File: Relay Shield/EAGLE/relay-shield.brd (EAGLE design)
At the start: 88.9 x 83.8 mm, 46 parts, among them J1 POWER_JACKSLT, Q1 MPSA42, Q2 MPSA42, Q3 MPSA42, Q4 MPSA42, U1 RELAYPANASONIC-JS, U2 RELAYPANASONIC-JS, U3 RELAYPANASONIC-JS, U4 RELAYPANASONIC-JS, U5 SPARK_CORE, U6 AP1509-50SG-13

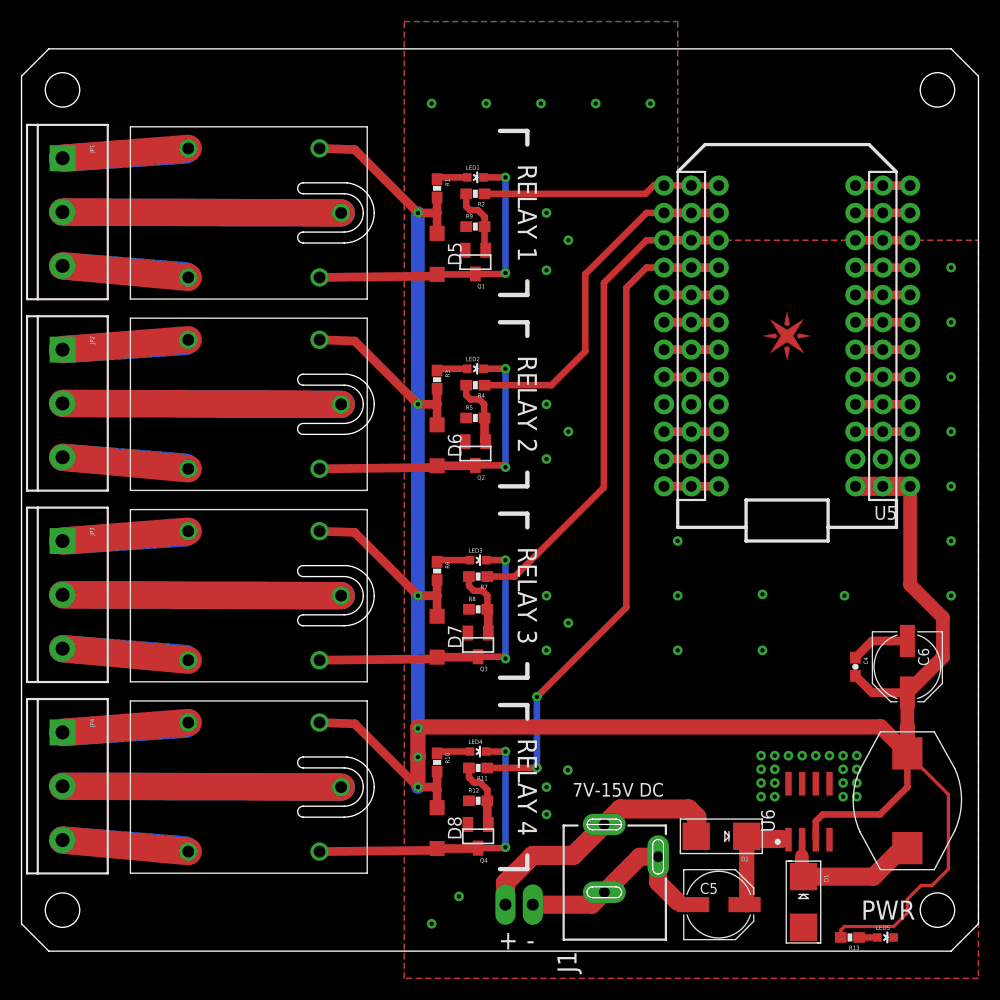
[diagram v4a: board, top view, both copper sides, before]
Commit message: updated relay shield files to v210
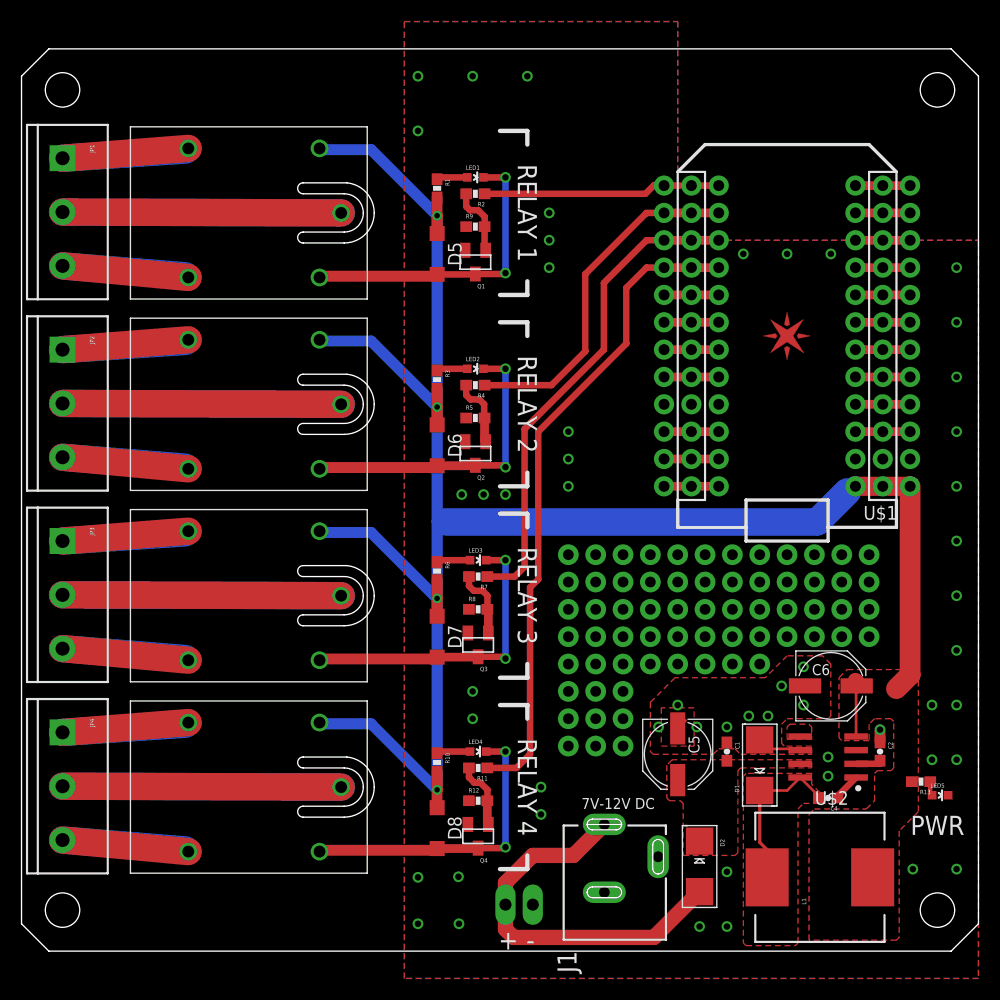
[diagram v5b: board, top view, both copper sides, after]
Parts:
- removed U6: AP1509-50SG-13, Spark:SO08
- added C1: 0.1uF, SparkFun-Capacitors:0603-CAP
- added C2: 10nF, SparkFun-Capacitors:0603-CAP
- added U$2: LM2672, Spark:SO08
- C5: value 47uF, 25V -> 100uF, 16V
- C6: value 100uF, 10V -> 56uF, 10V
- L1: value SDR1005-470KL -> CDRH125NP-470M; device Spark:INDUCTOR-SDR1005-470KL -> SparkFun-Passives:CDRH125
- moved R13 15.9 mm to (83.6, 15.7)
- moved C5 14.5 mm to (61.0, 18.3), turned to 270 degrees
- moved LED5 14.2 mm to (85.3, 14.5)
- moved D1 13.3 mm to (68.6, 17.3), turned to 90 degrees
- moved C4 12.5 mm to (74.9, 14.2), turned to 180 degrees
- moved L1 10.8 mm to (74.2, 6.86)
- moved C6 7.33 mm to (75.2, 24.6), turned to 0 degrees
- moved D2 3.45 mm to (63.0, 7.87), turned to 270 degrees
- renumbered U5 to U$1
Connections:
- new net N$33: C4.1, U$2.1
- new net N$35: U$2.5
- new net N$36: C2.2, U$2.2
- net +5V: now also L1.2, U$2.4; no longer C4.2, L1.P$2, U6.3
- net GND: now also C1.1, C2.1, U$2.6; no longer C4.1, U6.4, U6.5, U6.6, U6.7, U6.8
- net N$14: now also C1.2, U$2.7; no longer U6.1
- net N$34: now also C4.2, L1.1, U$2.8; no longer L1.P$1, U6.2
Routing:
- net +5V: track 257.8 -> 191.0 mm, vias 6 -> 4
- net GND: track 25.4 -> 7.21 mm, vias 52 -> 53
- net N$32: track 24.8 -> 35.9 mm
- net N$14: track 10.6 -> 0.52 mm
- net N$36: track 0.00 -> 2.91 mm
- net N$33: track 0.00 -> 2.78 mm
- net N$34: track 16.5 -> 15.2 mm
- net RELAY4: track 62.0 -> 60.9 mm, vias 2 -> 0
- added copper zone on layer 1, net +5V
- added copper zone on layer 1, net N$14
- added copper zone on layer 1, net N$34
- added copper zone on layer 1, net N$35
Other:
- board text added: "7V-12V DC"
- board text added: "Relay Shield v2.1.0 spark.io"
- board text removed: "7V-15V DC"
- board text removed: "Reference Designs ARE PROVIDED "AS IS" AND "WITH ALL FAULTS. SPARK LABS, INC ("SPARK") DISCLAIMS ALL OTHER WARRANTIES, EXPRESS OR IMPLIED, REGARDING PRODUCTS OR THE REFERENCE DESIGNS, INCLUDING BUT NOT LIMITED TO, ANY IMPLIED WARRANTIES OF MERCHANTABILITY, FITNESS FOR A PARTICULAR PURPOSE, OR NON-INFRINGEMENT. Spark may make changes to specifications and product descriptions at any time, without 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"
- board text removed: "Relay Shield v2.0.1 spark.io"

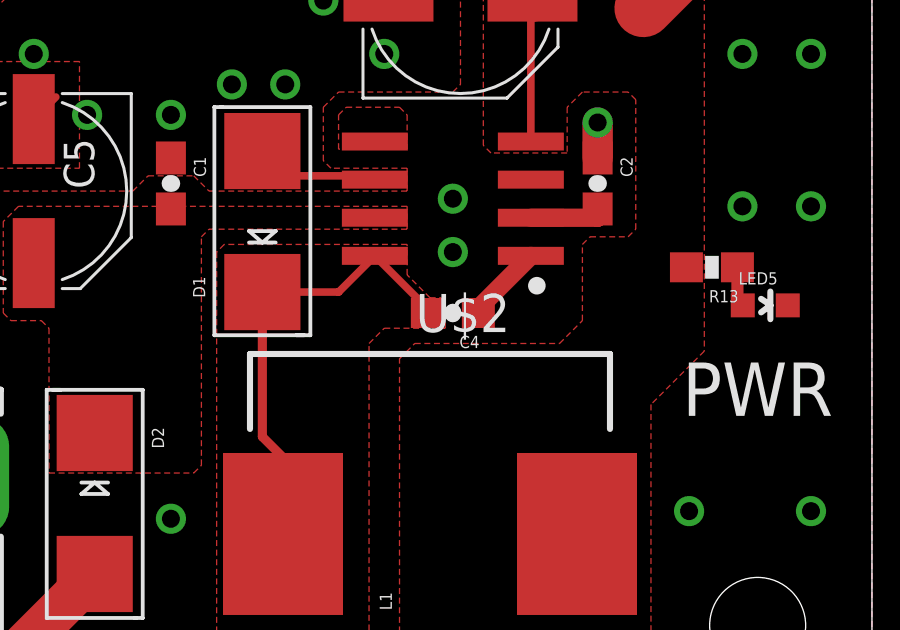
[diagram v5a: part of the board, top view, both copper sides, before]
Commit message: updated the bom and designator for regulator
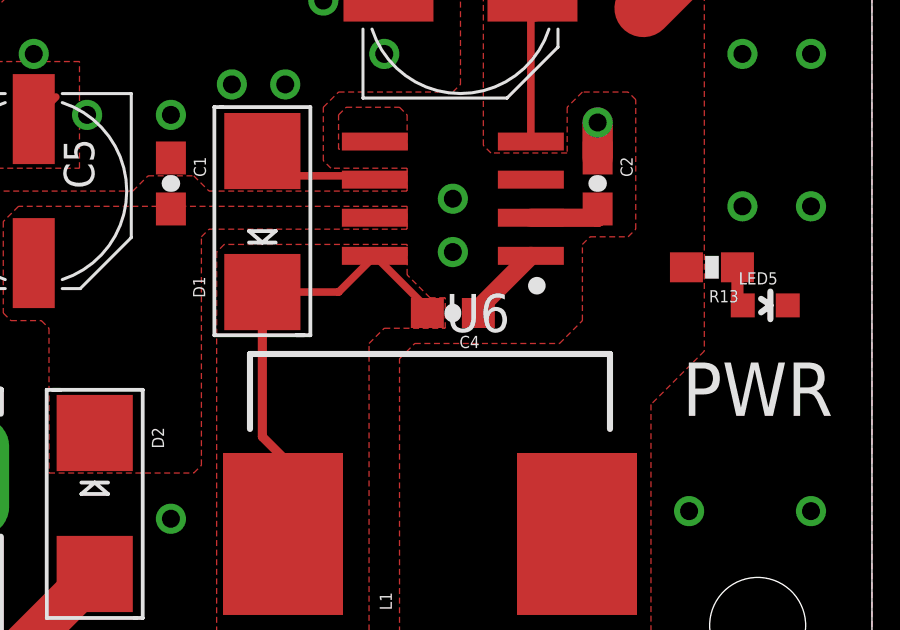
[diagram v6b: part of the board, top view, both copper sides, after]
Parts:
- renumbered U$2 to U6
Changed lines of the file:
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@@
 <element name="D1" library="adafruit" package="SMADIODE" value="B230" x="68.58" y="17.272" rot="R90"/>
 <element name="D2" library="adafruit" package="SMADIODE" value="B230" x="62.992" y="7.874" rot="R270"/>
-<element name="U$2" library="Spark" package="SO08" value="LM2672" x="74.93" y="18.034" rot="R90"/>
+<element name="U6" library="Spark" package="SO08" value="LM2672" x="74.93" y="18.034" rot="R90"/>
 <element name="C1" library="SparkFun-Capacitors" package="0603-CAP" value="0.1uF" x="65.532" y="18.542" rot="R270">
 <attribute name="PROD_ID" value="CAP-08604" x="65.532" y="18.542" size="1.778" layer="27" rot="R270" display="off"/>
@@
 <contactref element="Q3" pad="2"/>
 <contactref element="Q4" pad="2"/>
-<contactref element="U$2" pad="6"/>
-<contactref element="U$2" pad="6"/>
+<contactref element="U6" pad="6"/>
+<contactref element="U6" pad="6"/>
 <contactref element="C5" pad="-"/>
 <contactref element="J1" pad="GND@1"/>
@@
 <contactref element="D7" pad="C"/>
 <contactref element="D8" pad="C"/>
-<contactref element="U$2" pad="4"/>
+<contactref element="U6" pad="4"/>
 <contactref element="C6" pad="+"/>
 <contactref element="R13" pad="2"/>
@@
 <signal name="N$14">
 <contactref element="C5" pad="+"/>
-<contactref element="U$2" pad="7"/>
+<contactref element="U6" pad="7"/>
 <contactref element="D2" pad="C"/>
 <contactref element="C1" pad="2"/>
@@
 </signal>
 <signal name="N$33">
-<contactref element="U$2" pad="1"/>
+<contactref element="U6" pad="1"/>
 <contactref element="C4" pad="1"/>
 <wire x1="77.53" y1="15.974" x2="77.53" y2="16.129" width="0.254" layer="1"/>
@@
 </signal>
 <signal name="N$34">
-<contactref element="U$2" pad="8"/>
+<contactref element="U6" pad="8"/>
 <contactref element="D1" pad="C"/>
 <contactref element="C4" pad="2"/>
@@
 </signal>
 <signal name="N$35">
-<contactref element="U$2" pad="5"/>
+<contactref element="U6" pad="5"/>
 <polygon width="0" layer="1" spacing="6.4516" thermals="no">
 <vertex x="71.12" y="19.685"/>
@@
 <signal name="N$36">
 <contactref element="C2" pad="2"/>
-<contactref element="U$2" pad="2"/>
+<contactref element="U6" pad="2"/>
 <wire x1="80.01" y1="17.399" x2="79.756" y2="17.692" width="0.4064" layer="1"/>
 <wire x1="77.53" y1="17.399" x2="79.756" y2="17.399" width="0.6096" layer="1"/>

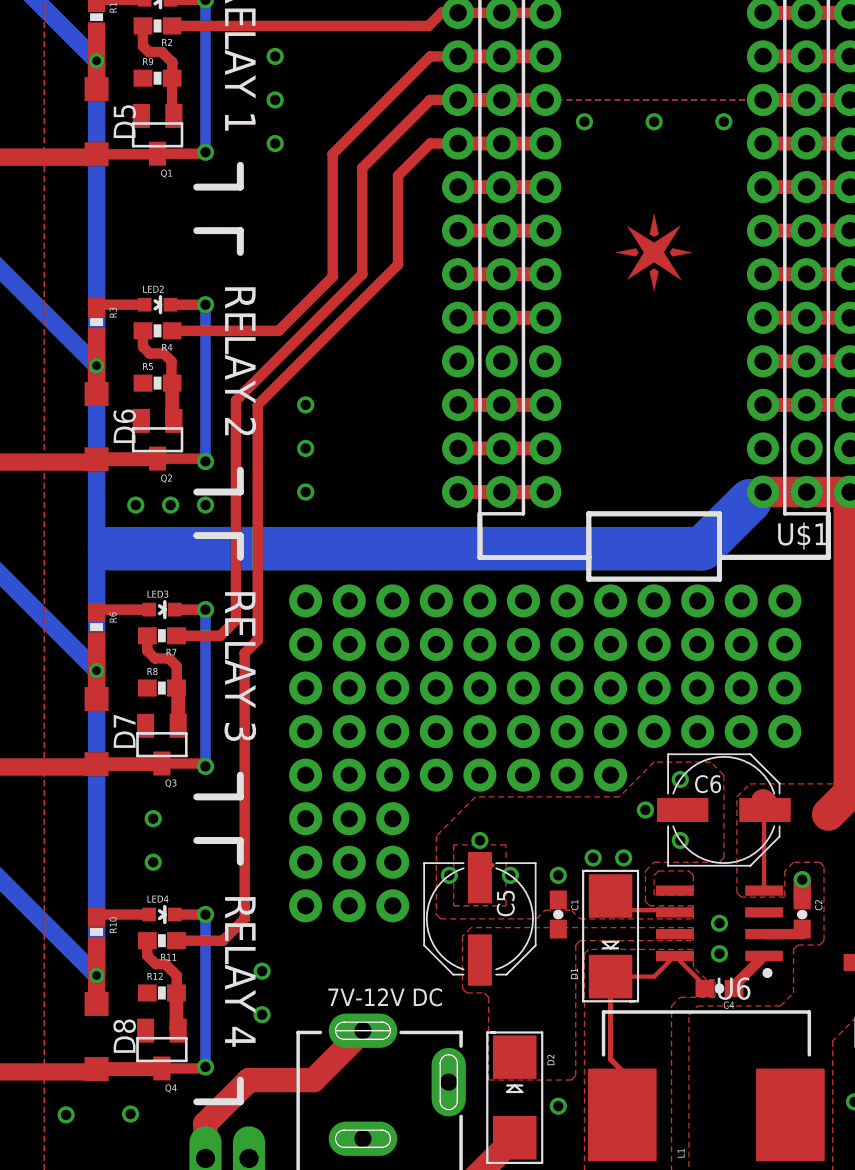
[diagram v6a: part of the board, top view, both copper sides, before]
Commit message: updated designators and bom
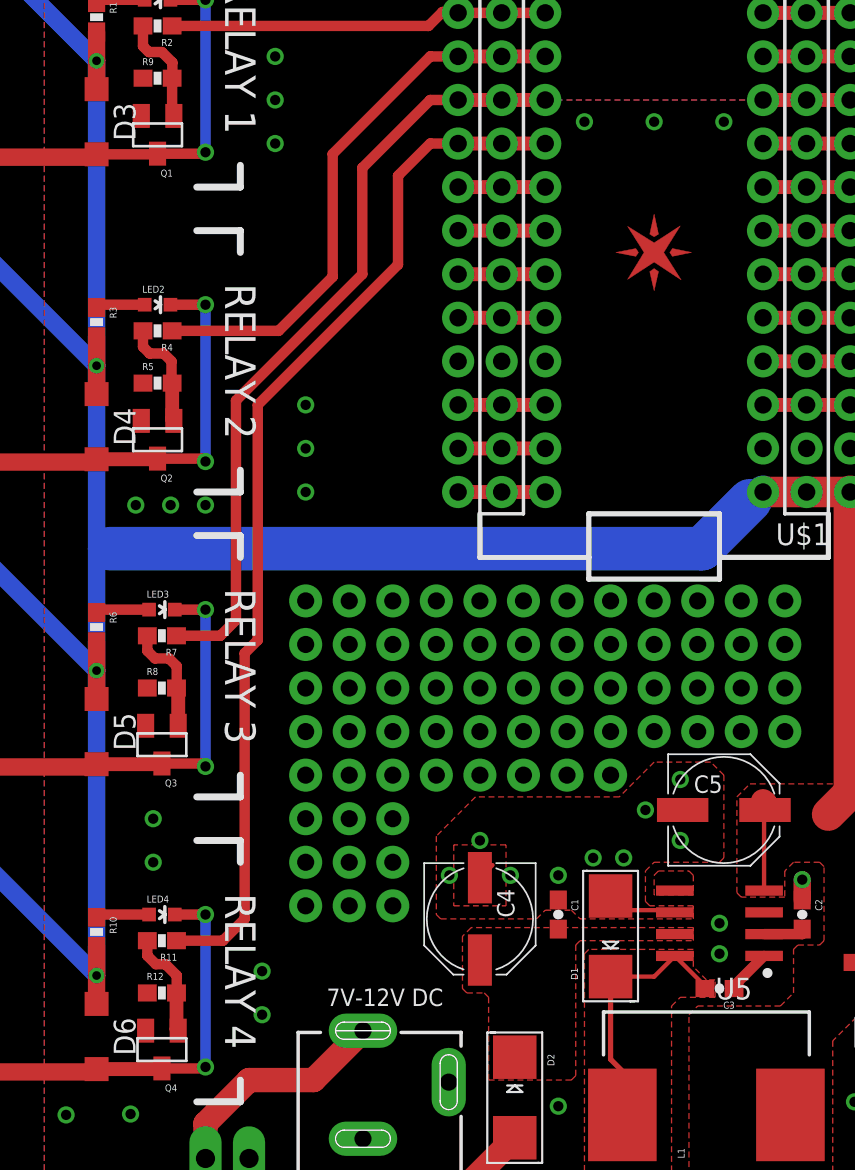
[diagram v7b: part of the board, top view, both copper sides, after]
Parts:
- removed C6: 56uF, 10V, SparkFun-Capacitors:PANASONIC_D
- removed D7, D8: (no value), diode:SOD123
- added C3: 10nF, SparkFun-Capacitors:0603-CAP
- added D3, D4: (no value), diode:SOD123
- C4: value 10nF -> 100uF, 16V; device SparkFun-Capacitors:0603-CAP -> SparkFun-Capacitors:PANASONIC_D
- C5: value 100uF, 16V -> 56uF, 10V
- moved D6 35.6 mm to (38.6, 11.4)
- moved D5 35.6 mm to (38.6, 29.2)
- moved C5 15.6 mm to (75.2, 24.6), turned to 0 degrees
- moved C4 14.5 mm to (61.0, 18.3), turned to 270 degrees
- renumbered U6 to U5
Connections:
- net +5V: now also C5.+, D3.C, D4.C; no longer C6.+, D7.C, D8.C
- net GND: now also C4.-; no longer C6.-
- net N$1: now also D3.A; no longer D5.A
- net N$11: now also D6.A; no longer D8.A
- net N$14: now also C4.+; no longer C5.+
- net N$33: now also C3.1; no longer C4.1
- net N$34: now also C3.2; no longer C4.2
- net N$5: now also D4.A; no longer D6.A
- net N$8: now also D5.A; no longer D7.A
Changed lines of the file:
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@@
 <attribute name="VALUE" value="MPSA42" x="42.418" y="10.668" size="1.778" layer="27" rot="R180" display="off"/>
 </element>
-<element name="D5" library="diode" package="SOD123" value="" x="38.608" y="64.77" rot="R270"/>
-<element name="D6" library="diode" package="SOD123" value="" x="38.608" y="46.99" rot="R270"/>
-<element name="D7" library="diode" package="SOD123" value="" x="38.608" y="29.21" rot="R270"/>
-<element name="D8" library="diode" package="SOD123" value="" x="38.608" y="11.43" rot="R270"/>
-<element name="C4" library="SparkFun-Capacitors" package="0603-CAP" value="10nF" x="74.93" y="14.224" rot="R180"/>
-<element name="C5" library="SparkFun-Capacitors" package="PANASONIC_D" value="100uF, 16V" x="60.96" y="18.288" rot="R270"/>
-<element name="C6" library="SparkFun-Capacitors" package="PANASONIC_D" value="56uF, 10V" x="75.184" y="24.638"/>
+<element name="D3" library="diode" package="SOD123" value="" x="38.608" y="64.77" rot="R270"/>
+<element name="D4" library="diode" package="SOD123" value="" x="38.608" y="46.99" rot="R270"/>
+<element name="D5" library="diode" package="SOD123" value="" x="38.608" y="29.21" rot="R270"/>
+<element name="D6" library="diode" package="SOD123" value="" x="38.608" y="11.43" rot="R270"/>
+<element name="C3" library="SparkFun-Capacitors" package="0603-CAP" value="10nF" x="74.93" y="14.224" rot="R180"/>
+<element name="C4" library="SparkFun-Capacitors" package="PANASONIC_D" value="100uF, 16V" x="60.96" y="18.288" rot="R270"/>
+<element name="C5" library="SparkFun-Capacitors" package="PANASONIC_D" value="56uF, 10V" x="75.184" y="24.638"/>
 <element name="D1" library="adafruit" package="SMADIODE" value="B230" x="68.58" y="17.272" rot="R90"/>
 <element name="D2" library="adafruit" package="SMADIODE" value="B230" x="62.992" y="7.874" rot="R270"/>
-<element name="U6" library="Spark" package="SO08" value="LM2672" x="74.93" y="18.034" rot="R90"/>
+<element name="U5" library="Spark" package="SO08" value="LM2672" x="74.93" y="18.034" rot="R90"/>
 <element name="C1" library="SparkFun-Capacitors" package="0603-CAP" value="0.1uF" x="65.532" y="18.542" rot="R270">
 <attribute name="PROD_ID" value="CAP-08604" x="65.532" y="18.542" size="1.778" layer="27" rot="R270" display="off"/>
@@
 <contactref element="Q3" pad="2"/>
 <contactref element="Q4" pad="2"/>
-<contactref element="U6" pad="6"/>
-<contactref element="U6" pad="6"/>
-<contactref element="C5" pad="-"/>
+<contactref element="U5" pad="6"/>
+<contactref element="U5" pad="6"/>
+<contactref element="C4" pad="-"/>
 <contactref element="J1" pad="GND@1"/>
 <contactref element="J1" pad="GND@2"/>
 <contactref element="D1" pad="A"/>
-<contactref element="C6" pad="-"/>
+<contactref element="C5" pad="-"/>
 <contactref element="JP5" pad="1"/>
 <via x="36.83" y="76.2" extent="1-16" drill="0.6"/>
@@
 <contactref element="R10" pad="2"/>
 <contactref element="U$1" pad="#1"/>
+<contactref element="D3" pad="C"/>
+<contactref element="D4" pad="C"/>
 <contactref element="D5" pad="C"/>
 <contactref element="D6" pad="C"/>
-<contactref element="D7" pad="C"/>
-<contactref element="D8" pad="C"/>
-<contactref element="U6" pad="4"/>
-<contactref element="C6" pad="+"/>
+<contactref element="U5" pad="4"/>
+<contactref element="C5" pad="+"/>
 <contactref element="R13" pad="2"/>
 <wire x1="82.55" y1="43.18" x2="80.01" y2="43.18" width="1.778" layer="1"/>
@@
 <contactref element="LED1" pad="C"/>
 <contactref element="Q1" pad="3"/>
-<contactref element="D5" pad="A"/>
+<contactref element="D3" pad="A"/>
 <wire x1="42.164" y1="62.908" x2="42.126" y2="62.87" width="0.6096" layer="1"/>
 <wire x1="42.126" y1="62.87" x2="38.608" y2="62.87" width="0.6096" layer="1"/>
@@
 <contactref element="LED2" pad="C"/>
 <contactref element="Q2" pad="3"/>
-<contactref element="D6" pad="A"/>
+<contactref element="D4" pad="A"/>
 <wire x1="38.443" y1="44.925" x2="38.608" y2="45.09" width="0.8128" layer="1"/>
 <wire x1="38.608" y1="45.09" x2="42.126" y2="45.09" width="0.8128" layer="1"/>
@@
 <contactref element="LED3" pad="C"/>
 <contactref element="Q3" pad="3"/>
-<contactref element="D7" pad="A"/>
+<contactref element="D5" pad="A"/>
 <wire x1="38.443" y1="27.145" x2="38.608" y2="27.31" width="0.8128" layer="1"/>
 <wire x1="38.608" y1="27.31" x2="42.38" y2="27.31" width="0.8128" layer="1"/>
@@
 <contactref element="LED4" pad="C"/>
 <contactref element="Q4" pad="3"/>
-<contactref element="D8" pad="A"/>
+<contactref element="D6" pad="A"/>
 <wire x1="38.443" y1="9.365" x2="38.608" y2="9.53" width="0.8128" layer="1"/>
 <wire x1="38.608" y1="9.53" x2="42.38" y2="9.53" width="0.8128" layer="1"/>
@@
 </signal>
 <signal name="N$14">
-<contactref element="C5" pad="+"/>
-<contactref element="U6" pad="7"/>
+<contactref element="C4" pad="+"/>
+<contactref element="U5" pad="7"/>
 <contactref element="D2" pad="C"/>
 <contactref element="C1" pad="2"/>
@@
 </signal>
 <signal name="N$33">
-<contactref element="U6" pad="1"/>
-<contactref element="C4" pad="1"/>
+<contactref element="U5" pad="1"/>
+<contactref element="C3" pad="1"/>
 <wire x1="77.53" y1="15.974" x2="77.53" y2="16.129" width="0.254" layer="1"/>
 <wire x1="75.78" y1="14.224" x2="75.78" y2="14.379" width="0.6096" layer="1"/>
@@
 </signal>
 <signal name="N$34">
-<contactref element="U6" pad="8"/>
+<contactref element="U5" pad="8"/>
 <contactref element="D1" pad="C"/>
-<contactref element="C4" pad="2"/>
+<contactref element="C3" pad="2"/>
 <contactref element="L1" pad="1"/>
 <wire x1="69.268" y1="6.858" x2="69.268" y2="9.412" width="0.254" layer="1"/>
@@
 </signal>
 <signal name="N$35">
-<contactref element="U6" pad="5"/>
+<contactref element="U5" pad="5"/>
 <polygon width="0" layer="1" spacing="6.4516" thermals="no">
 <vertex x="71.12" y="19.685"/>
@@
 <signal name="N$36">
 <contactref element="C2" pad="2"/>
-<contactref element="U6" pad="2"/>
+<contactref element="U5" pad="2"/>
 <wire x1="80.01" y1="17.399" x2="79.756" y2="17.692" width="0.4064" layer="1"/>
 <wire x1="77.53" y1="17.399" x2="79.756" y2="17.399" width="0.6096" layer="1"/>
